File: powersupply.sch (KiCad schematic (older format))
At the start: 19 parts, among them P1 PWR, P2 PWR_SW, U1 LM7805, U2 LM3940

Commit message: Fixes #6: removes SWR measurement voltage divider
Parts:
- U2: footprint nu9j-footprints:TO-263_VIVOGND -> SMD_Packages:SOT-223
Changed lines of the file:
@@
 F 0 "U2" H 5900 3804 60  0000 C CNN
 F 1 "LM3940" H 5750 4200 60  0000 C CNN
-F 2 "nu9j-footprints:TO-263_VIVOGND" H 5750 4000 60  0001 C CNN
+F 2 "SMD_Packages:SOT-223" H 5750 4000 60  0001 C CNN
 F 3 "" H 5750 4000 60  0000 C CNN
 	1    5750 4000

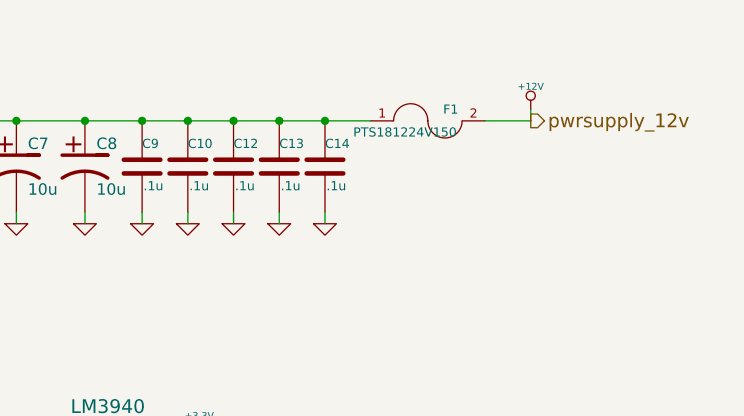
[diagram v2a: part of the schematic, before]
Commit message: Fixes #10: resettable fuse trips too easily
Replaced fuse with PTS18128V200 that has a hold current of 2.0A
instead of 1.5A.
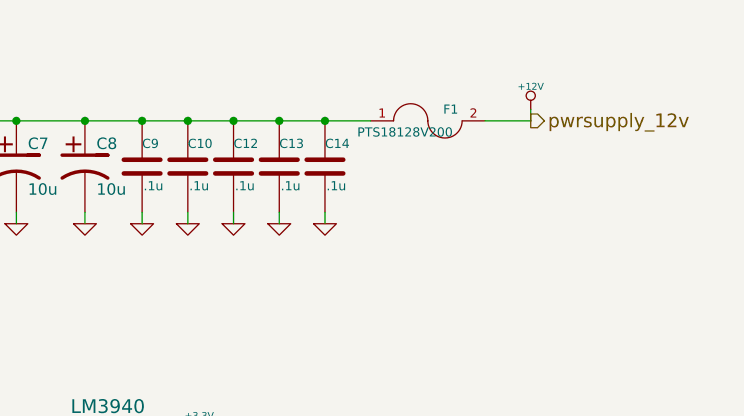
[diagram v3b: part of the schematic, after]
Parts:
- F1: value PTS181224V150 -> PTS18128V200
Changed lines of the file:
@@
 P 7150 2550
 F 0 "F1" H 7250 2600 40  0000 C CNN
-F 1 "PTS181224V150" H 7050 2500 40  0000 C CNN
+F 1 "PTS18128V200" H 7050 2500 40  0000 C CNN
 F 2 "SMD_Packages:SMD-1812_l" H 7150 2550 60  0001 C CNN
 F 3 "" H 7150 2550 60  0000 C CNN

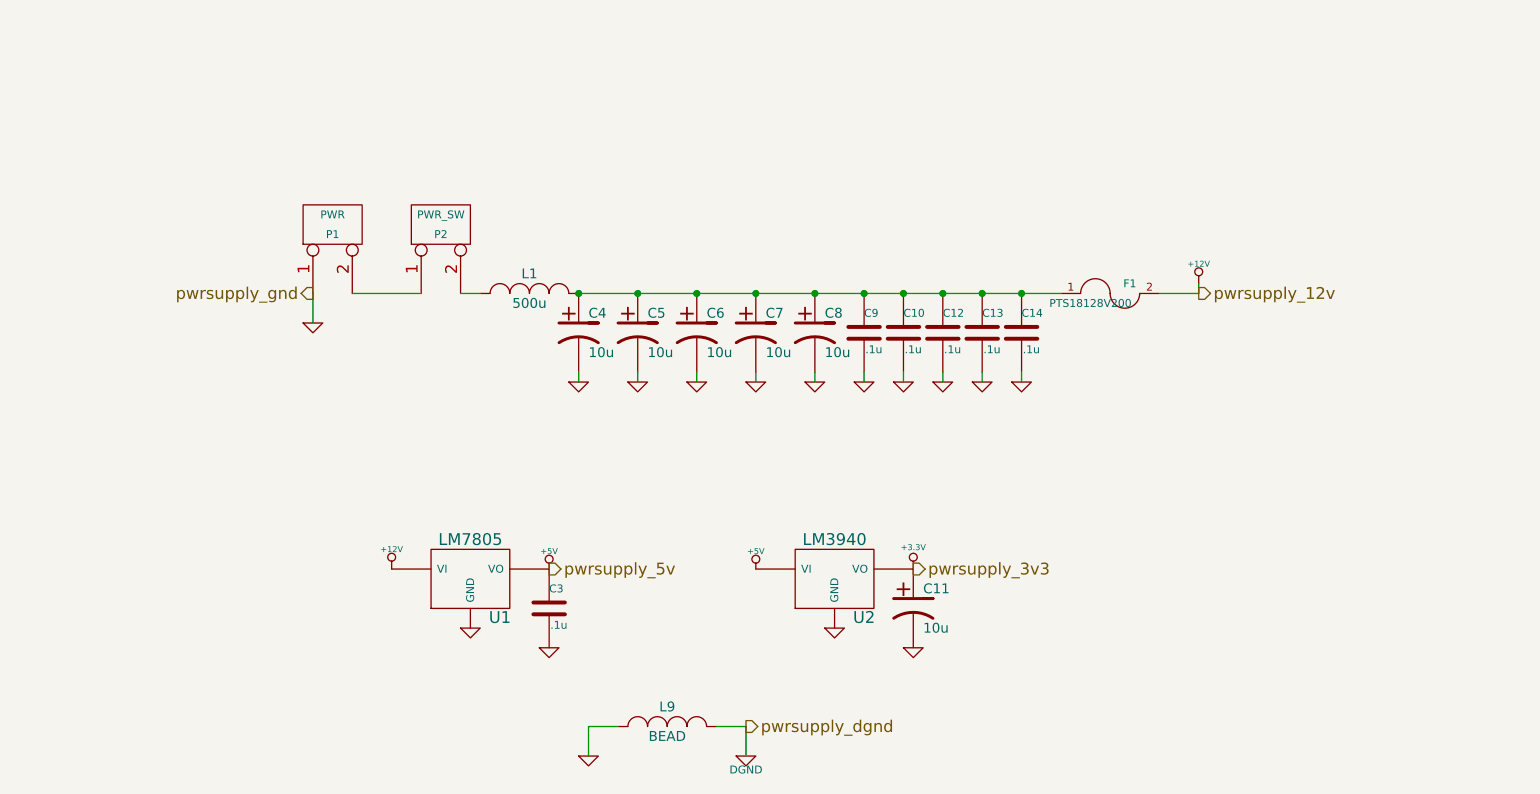
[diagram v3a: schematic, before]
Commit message: Fixes #8: transistor placement
Also, this is a major board layout change

- Added more 12V filtering caps
- Placed fuse in front of filtering caps
- Changed IRF510 footprints to horizontal lower side w/ mounting hole
- Expanded layout to fill new board size
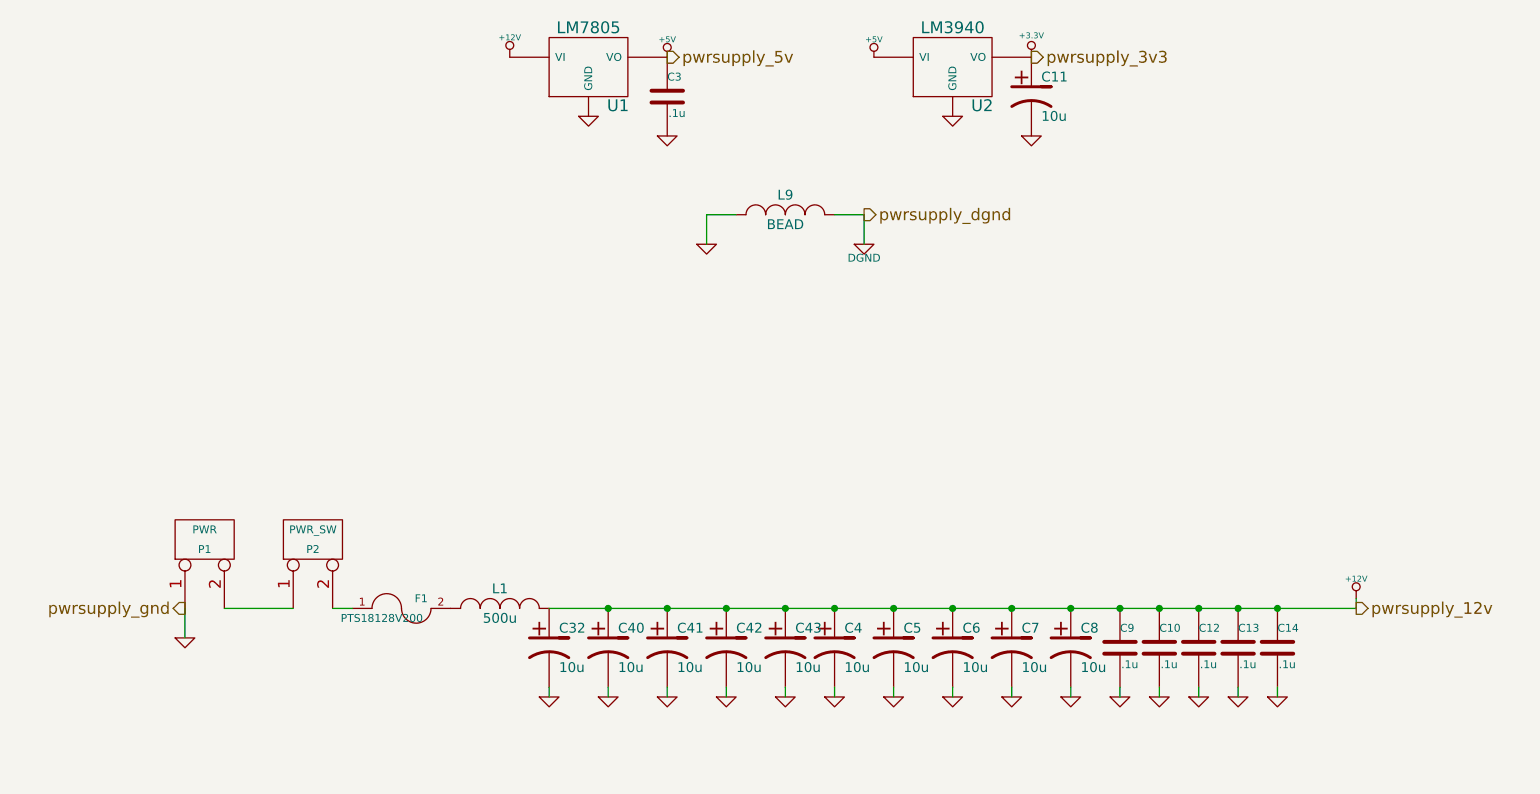
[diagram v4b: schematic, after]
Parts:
- added C32, C40, C41, C42, C43: 10u, Capacitors_ThroughHole:C_Radial_D5_L11_P2.5, symbol CP1
- C4, C5, C6, C7, C8: footprint Capacitors_ThroughHole:Capacitor5x11RM2.5 -> Capacitors_ThroughHole:C_Radial_D5_L11_P2.5
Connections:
- net +12V: now also C10.1, C12.1, C13.1, C14.1, C4.1, C5.1, C6.1, C7.1, C8.1, C9.1, L1.2, C32.1, C40.1, C41.1, C42.1, C43.1; no longer F1.2
- net GND: now also C32.2, C40.2, C41.2, C42.2, C43.2
- net at P2.2 (PM): now also F1.1; no longer L1.1
- new net: F1.2, L1.1
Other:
- moved on the sheet: C10, C11, C12, C13, C14, C3, C4, C5, C6, C7, C8, C9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
